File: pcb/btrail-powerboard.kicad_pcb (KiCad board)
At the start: 2 copper layers, 33.5 x 27.5 mm, 10 parts, among them J1 RJ45 Shielded, Q1 BC328, Q2 BC328, U2 XL1509-5.0

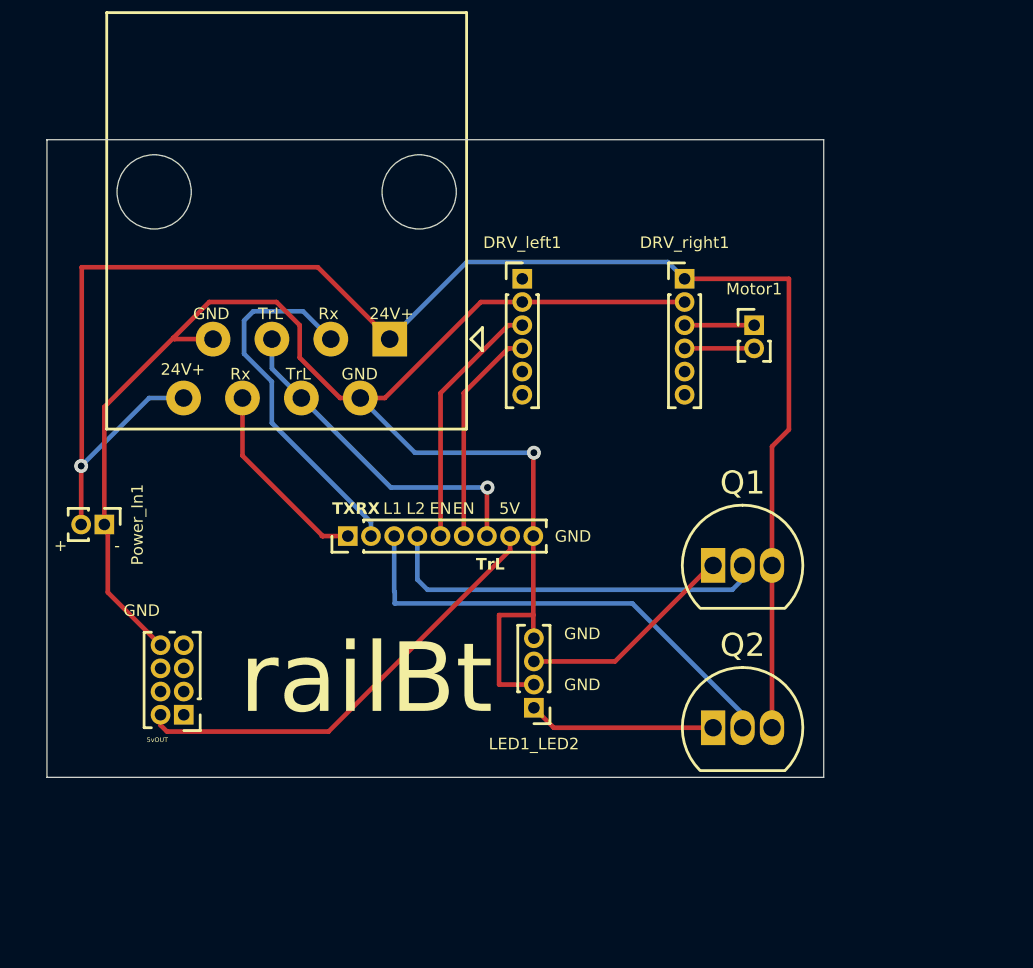
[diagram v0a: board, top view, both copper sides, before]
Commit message: Update railBT board with sockets for H-bridge and 5V buck converter
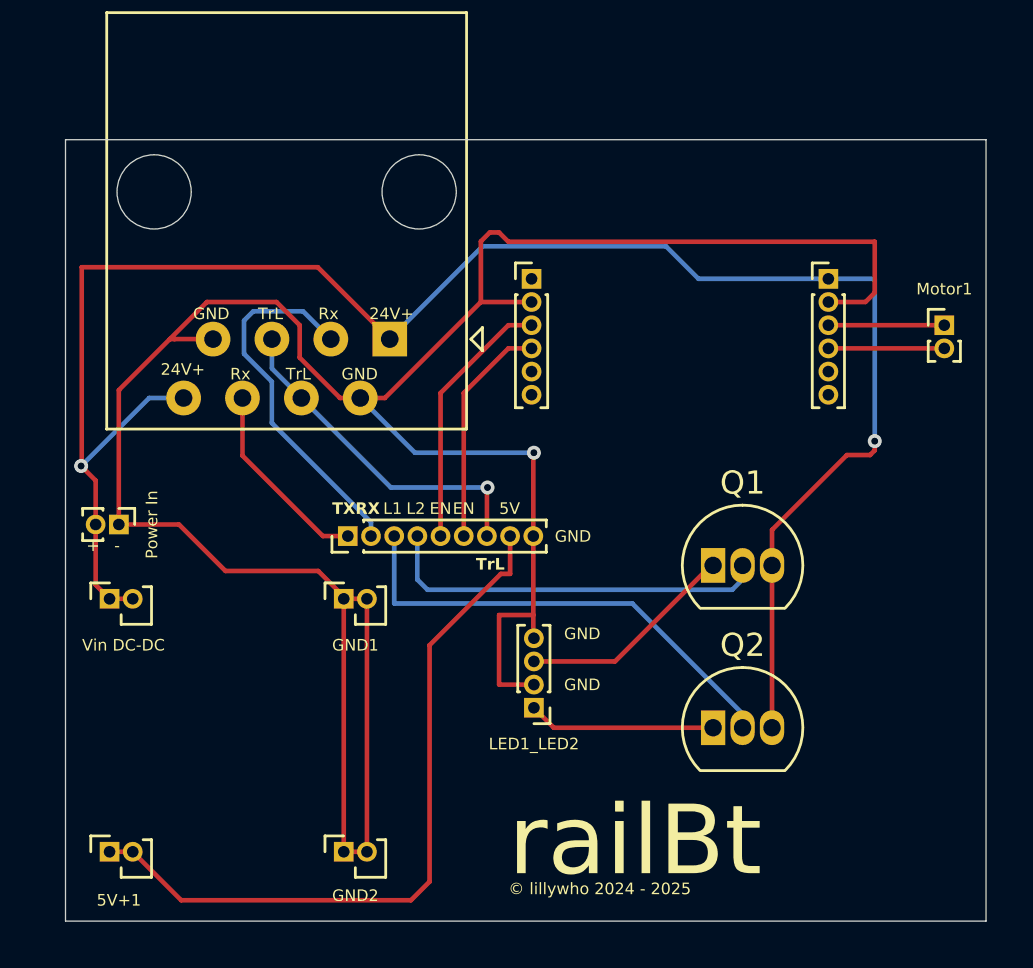
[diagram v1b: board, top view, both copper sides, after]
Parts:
- removed U2: XL1509-5.0, Connector_PinHeader_1.00mm:PinHeader_2x04_P1.00mm_Vertical
- added 5V+1: Conn_01x02, Connector_PinSocket_1.00mm:PinSocket_1x02_P1.00mm_Vertical, F.Cu at (194.2, 52.7)
- added GND1: Conn_01x02, Connector_PinSocket_1.00mm:PinSocket_1x02_P1.00mm_Vertical, F.Cu at (204.3, 41.8)
- added GND2: Conn_01x02, Connector_PinSocket_1.00mm:PinSocket_1x02_P1.00mm_Vertical, F.Cu at (204.3, 52.7)
- added Vin DC-DC: Conn_01x01, Connector_PinSocket_1.00mm:PinSocket_1x02_P1.00mm_Vertical, F.Cu at (194.2, 41.8)
- J1: value RJ45 Shielded -> RJ45_Shielded
- Power In: renamed from Power_In1
- moved Motor1 8.20 mm to (230.2, 30.0)
- moved DRV_right1 6.20 mm to (225.2, 28.0)
- moved Power In 0.62 mm to (194.6, 38.6)
- moved DRV_left1 0.40 mm to (212.4, 28.0)
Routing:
- net Net-(DRV_left1-Pin_2): track 66.6 -> 113.0 mm
- net Net-(5V+1-Pin_1): track 19.5 -> 31.6 mm
- net Net-(DRV_right1-Pin_1): track 69.9 -> 81.0 mm, vias 1 -> 2
- net Net-(DRV_right1-Pin_4): track 3.00 -> 5.00 mm
- net Net-(DRV_right1-Pin_3): track 3.00 -> 5.00 mm
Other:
- board size 33.5 x 27.5 mm -> 39.7 x 33.7 mm
- board text added: "© lillywho 2024 - 2025"
- board text removed: "5vOUT"

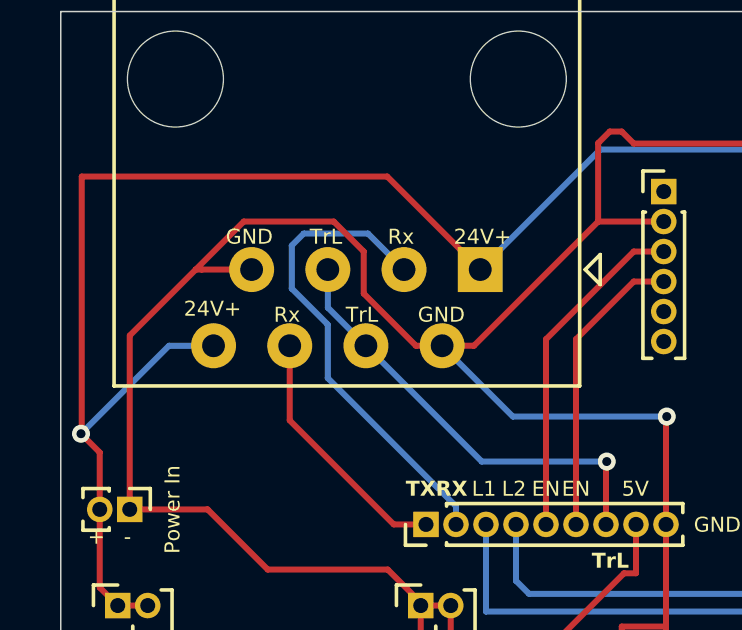
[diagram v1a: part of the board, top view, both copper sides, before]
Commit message: Fix labelling on TX Pin
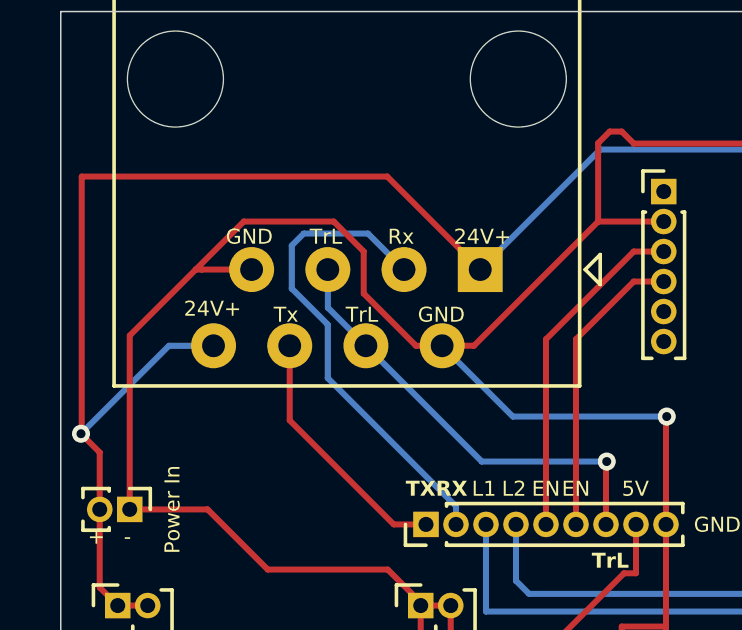
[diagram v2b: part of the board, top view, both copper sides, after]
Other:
- board text added: "Tx"
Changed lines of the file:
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@@
 		)
 	)
-	(gr_text "Rx"
+	(gr_text "Tx"
 		(at 200.4 32.4 0)
 		(layer "B.SilkS")
@@
 		)
 	)
-	(gr_text "Rx"
+	(gr_text "Tx"
 		(at 199.4 32.4 0)
 		(layer "F.SilkS")

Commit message: Remove unnecessary vias
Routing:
- net Net-(DRV_right1-Pin_1): track 81.0 -> 77.6 mm, vias 2 -> 1
- net Net-(DRV_left1-Pin_2): track 113.0 -> 112.3 mm, vias 1 -> 0
- net Net-(ESP32_jack1-Pin_7): vias 1 -> 0
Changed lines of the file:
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@@
 			(layer "F.Fab")
 		)
-		(fp_text user "${REFERENCE}"
-			(at -0.29 0.5 360)
-			(layer "F.Fab")
-			(effects
-				(font
-					(size 0.9 0.9)
-					(thickness 0.14)
-				)
-			)
-		)
 		(pad "1" thru_hole rect
 			(at 0 0 90)
@@
 			(layer "F.Fab")
 		)
-		(fp_text user "${REFERENCE}"
-			(at -0.29 0.5 360)
-			(layer "F.Fab")
-			(effects
-				(font
-					(size 0.9 0.9)
-					(thickness 0.14)
-				)
-			)
-		)
 		(pad "1" thru_hole rect
 			(at 0 0 90)
@@
 			(layer "F.Fab")
 		)
-		(fp_text user "${REFERENCE}"
-			(at -0.29 0.5 360)
-			(layer "F.Fab")
-			(effects
-				(font
-					(size 0.9 0.9)
-					(thickness 0.14)
-				)
-			)
-		)
 		(pad "1" thru_hole rect
 			(at 0 0 90)
@@
 	)
 	(segment
-		(start 212.5 35.5)
-		(end 212.475 35.525)
-		(width 0.2)
-		(layer "F.Cu")
-		(net 2)
-	)
-	(segment
 		(start 210.21316 29)
 		(end 210.21316 26.38684)
@@
 	)
 	(segment
-		(start 212.475 39.095)
-		(end 212.475 35.525)
-		(width 0.2)
-		(layer "F.Cu")
-		(net 2)
-	)
-	(segment
 		(start 205.3 41.8)
 		(end 204.3 41.8)
@@
 		(net 2)
 	)
-	(via
-		(at 212.5 35.5)
-		(size 0.6)
-		(drill 0.3)
-		(layers "F.Cu" "B.Cu")
+	(segment
+		(start 208.94 33.14)
+		(end 205.0125 33.14)
+		(width 0.2)
+		(layer "B.Cu")
 		(net 2)
 	)
 	(segment
-		(start 212.5 35.5)
-		(end 207.3725 35.5)
+		(start 212.475 39.095)
+		(end 212.475 36.675)
 		(width 0.2)
 		(layer "B.Cu")
@@
 	)
 	(segment
-		(start 207.3725 35.5)
-		(end 205.0125 33.14)
+		(start 212.475 36.675)
+		(end 208.94 33.14)
 		(width 0.2)
 		(layer "B.Cu")
@@
 	)
 	(segment
+		(start 225.174695 28)
+		(end 225.2 28)
+		(width 0.2)
+		(layer "F.Cu")
+		(net 10)
+	)
+	(segment
 		(start 193.6 38.595)
 		(end 193.6 41.2)
@@
 	)
 	(segment
-		(start 227.2 35.4)
-		(end 227 35.6)
+		(start 222.77 40.36)
+		(end 222.77 38.83)
 		(width 0.2)
 		(layer "F.Cu")
@@
 	)
 	(segment
-		(start 226 35.6)
-		(end 222.77 38.83)
+		(start 222.77 38.83)
+		(end 222.8 38.8)
 		(width 0.2)
 		(layer "F.Cu")
@@
 	)
 	(segment
-		(start 227.2 35)
-		(end 227.2 35.4)
+		(start 222.8 30.374695)
+		(end 225.174695 28)
 		(width 0.2)
 		(layer "F.Cu")
@@
 	)
 	(segment
+		(start 222.8 38.8)
+		(end 222.8 30.374695)
+		(width 0.2)
+		(layer "F.Cu")
+		(net 10)
+	)
+	(segment
 		(start 193 27.5)
 		(end 203.1825 27.5)
@@
 	)
 	(segment
-		(start 222.77 38.83)
-		(end 222.77 40.36)
-		(width 0.2)
-		(layer "F.Cu")
-		(net 10)
-	)
-	(segment
-		(start 227 35.6)
-		(end 226 35.6)
-		(width 0.2)
-		(layer "F.Cu")
-		(net 10)
-	)
-	(segment
 		(start 203.1825 27.5)
 		(end 206.2825 30.6)
@@
 	)
 	(via
-		(at 227.2 35)
-		(size 0.6)
-		(drill 0.3)
-		(layers "F.Cu" "B.Cu")
-		(net 10)
-	)
-	(via
 		(at 192.975 36.072575)
 		(size 0.6)
@@
 	)
 	(segment
-		(start 227.2 28)
-		(end 227.2 35)
-		(width 0.2)
-		(layer "B.Cu")
-		(net 10)
-	)
-	(segment
 		(start 210.2825 26.6)
 		(end 218.2 26.6)
@@
 	)
 	(segment
-		(start 227.2 28)
-		(end 225.2 28)
+		(start 201.2025 31.87)
+		(end 202.4725 33.14)
 		(width 0.2)
 		(layer "B.Cu")
-		(net 10)
-	)
-	(segment
-		(start 210.475 37.025)
-		(end 210.5 37)
-		(width 0.2)
-		(layer "F.Cu")
 		(net 12)
 	)
 	(segment
-		(start 210.475 39.095)
-		(end 210.475 37.025)
+		(start 201.2025 30.6)
+		(end 201.2025 31.87)
 		(width 0.2)
-		(layer "F.Cu")
-		(net 12)
-	)
-	(via
-		(at 210.5 37)
-		(size 0.6)
-		(drill 0.3)
-		(layers "F.Cu" "B.Cu")
+		(layer "B.Cu")
 		(net 12)
 	)
 	(segment
-		(start 201.2025 31.87)
-		(end 202.4725 33.14)
+		(start 210.5 37)
+		(end 206.3325 37)
 		(width 0.2)
 		(layer "B.Cu")
@@
 	)
 	(segment
-		(start 201.2025 30.6)
-		(end 201.2025 31.87)
+		(start 210.5 37)
+		(end 210.475 37.025)
 		(width 0.2)
 		(layer "B.Cu")
@@
 	)
 	(segment
-		(start 210.5 37)
-		(end 206.3325 37)
+		(start 206.3325 37)
+		(end 202.4725 33.14)
 		(width 0.2)
 		(layer "B.Cu")
@@
 	)
 	(segment
-		(start 206.3325 37)
-		(end 202.4725 33.14)
+		(start 210.475 37.025)
+		(end 210.475 39.095)
 		(width 0.2)
 		(layer "B.Cu")

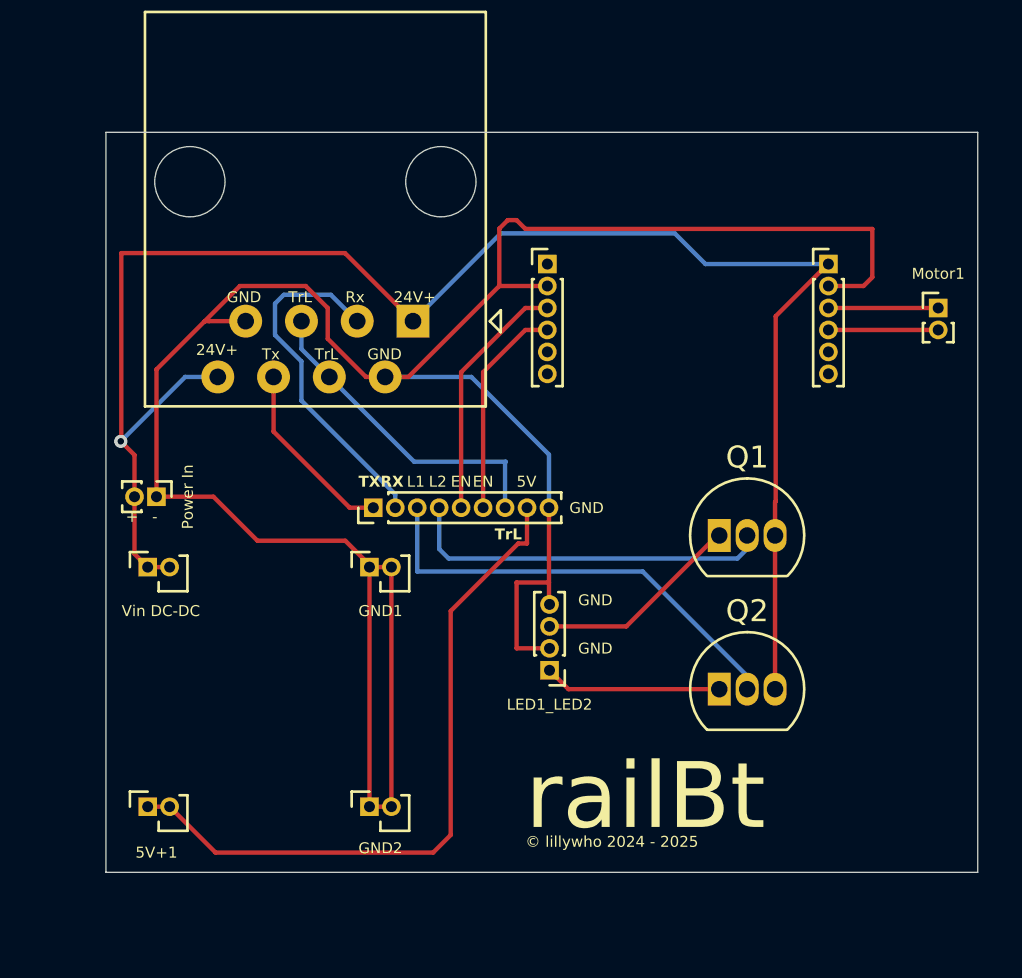
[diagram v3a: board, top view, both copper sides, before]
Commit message: Add mounting holes to power board
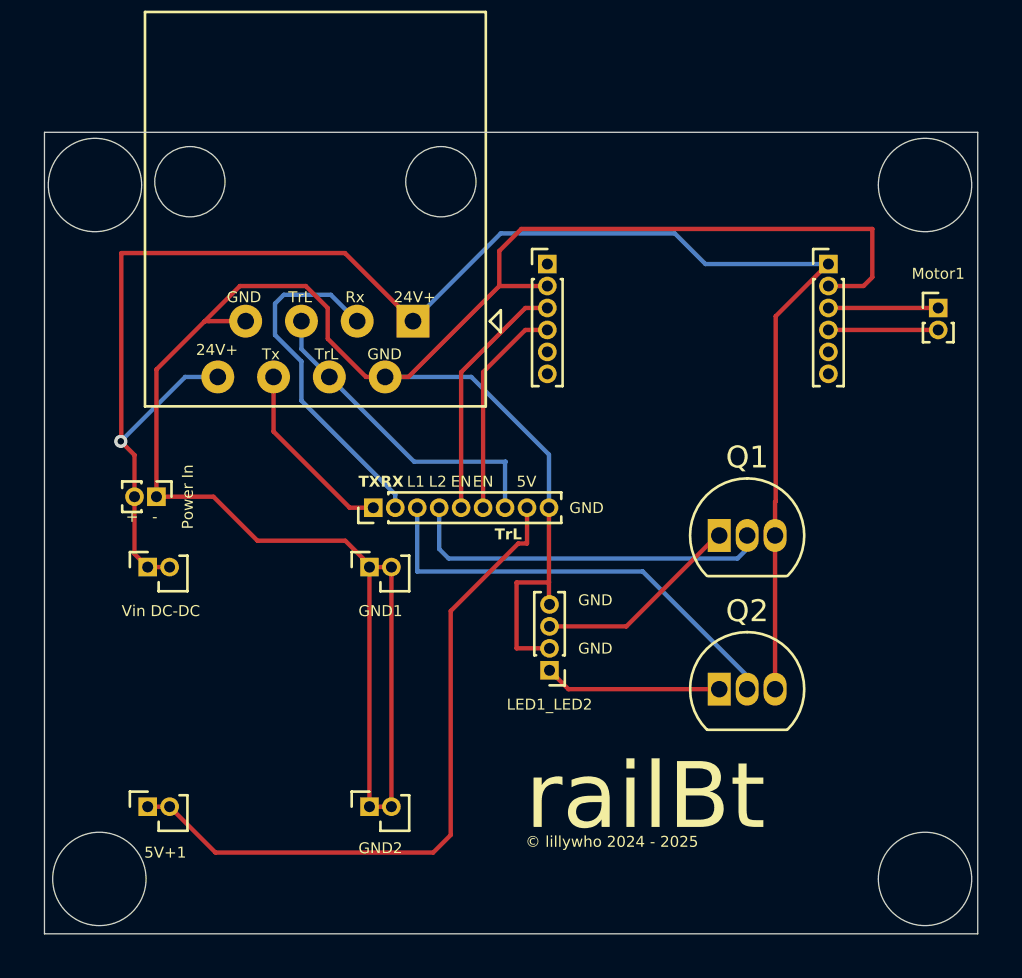
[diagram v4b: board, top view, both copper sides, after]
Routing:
- net Net-(DRV_left1-Pin_2): track 112.3 -> 111.4 mm
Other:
- board size 39.7 x 33.7 mm -> 42.5 x 36.5 mm
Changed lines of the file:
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@@
 		(tags "Through hole socket strip THT 1x02 1.00mm single row")
 		(property "Reference" "5V+1"
-			(at -2.09 0.4 180)
+			(at -2.09 0.8 180)
 			(layer "F.SilkS")
 			(effects
@@
 		)
 	)
+	(gr_circle
+		(center 192 56)
+		(end 190.6 54.4)
+		(stroke
+			(width 0.05)
+			(type default)
+		)
+		(fill none)
+		(layer "Edge.Cuts")
+	)
 	(gr_rect
-		(start 192.3 22)
-		(end 232 55.7)
+		(start 189.5 22)
+		(end 232 58.5)
+		(stroke
+			(width 0.05)
+			(type default)
+		)
+		(fill none)
+		(layer "Edge.Cuts")
+	)
+	(gr_circle
+		(center 229.6 56)
+		(end 228.2 54.4)
+		(stroke
+			(width 0.05)
+			(type default)
+		)
+		(fill none)
+		(layer "Edge.Cuts")
+	)
+	(gr_circle
+		(center 229.6 24.4)
+		(end 228.2 22.8)
+		(stroke
+			(width 0.05)
+			(type default)
+		)
+		(fill none)
+		(layer "Edge.Cuts")
+	)
+	(gr_circle
+		(center 191.8 24.4)
+		(end 190.4 22.8)
 		(stroke
 			(width 0.05)
@@
 	)
 	(segment
-		(start 210.21316 29)
-		(end 210.21316 26.38684)
-		(width 0.2)
-		(layer "F.Cu")
-		(net 2)
-	)
-	(segment
 		(start 204.3 52.71)
 		(end 205.3 52.71)
@@
 	)
 	(segment
-		(start 226.8 29)
-		(end 225.2 29)
-		(width 0.2)
-		(layer "F.Cu")
-		(net 2)
-	)
-	(segment
 		(start 206.07316 33.14)
 		(end 210.21316 29)
@@
 	)
 	(segment
-		(start 227.2 26.4)
-		(end 227.2 28.6)
-		(width 0.2)
-		(layer "F.Cu")
-		(net 2)
-	)
-	(segment
 		(start 202.4 31.399999)
 		(end 202.4 30)
@@
 	)
 	(segment
+		(start 227.2 26.4)
+		(end 211.21316 26.4)
+		(width 0.2)
+		(layer "F.Cu")
+		(net 2)
+	)
+	(segment
 		(start 198.4 29)
 		(end 196.8 30.6)
@@
 	)
 	(segment
-		(start 211 26)
-		(end 211.4 26.4)
+		(start 227.2 28.6)
+		(end 227.2 26.4)
 		(width 0.2)
 		(layer "F.Cu")
@@
 	)
 	(segment
+		(start 210.21316 27.4)
+		(end 210.21316 29)
+		(width 0.2)
+		(layer "F.Cu")
+		(net 2)
+	)
+	(segment
+		(start 226.8 29)
+		(end 227.2 28.6)
+		(width 0.2)
+		(layer "F.Cu")
+		(net 2)
+	)
+	(segment
 		(start 204.3 52.71)
 		(end 204.3 41.8)
@@
 	)
 	(segment
-		(start 210.6 26)
-		(end 211 26)
-		(width 0.2)
-		(layer "F.Cu")
-		(net 2)
-	)
-	(segment
-		(start 227.2 28.6)
-		(end 226.8 29)
-		(width 0.2)
-		(layer "F.Cu")
-		(net 2)
-	)
-	(segment
 		(start 205.0125 33.14)
 		(end 204.140001 33.14)
@@
 	)
 	(segment
+		(start 211.21316 26.4)
+		(end 210.21316 27.4)
+		(width 0.2)
+		(layer "F.Cu")
+		(net 2)
+	)
+	(segment
 		(start 201.4 29)
 		(end 198.4 29)
@@
 	)
 	(segment
+		(start 225.2 29)
+		(end 226.8 29)
+		(width 0.2)
+		(layer "F.Cu")
+		(net 2)
+	)
+	(segment
 		(start 199.2 40.6)
 		(end 203.2 40.6)
@@
 	)
 	(segment
-		(start 211.4 26.4)
-		(end 227.2 26.4)
-		(width 0.2)
-		(layer "F.Cu")
-		(net 2)
-	)
-	(segment
 		(start 212.475 39.095)
 		(end 212.475 42.5)
 		(width 0.2)
 		(layer "F.Cu")
-		(net 2)
-	)
-	(segment
-		(start 210.21316 26.38684)
-		(end 210.6 26)
-		(width 0.2)
-		(layer "F.Cu")
